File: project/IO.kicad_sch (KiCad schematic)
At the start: 15 parts, among them SW1 CARRIER, SW2 PORT B, SW3 INTERRUPT, X1 PORT B, X2 EXPANSION

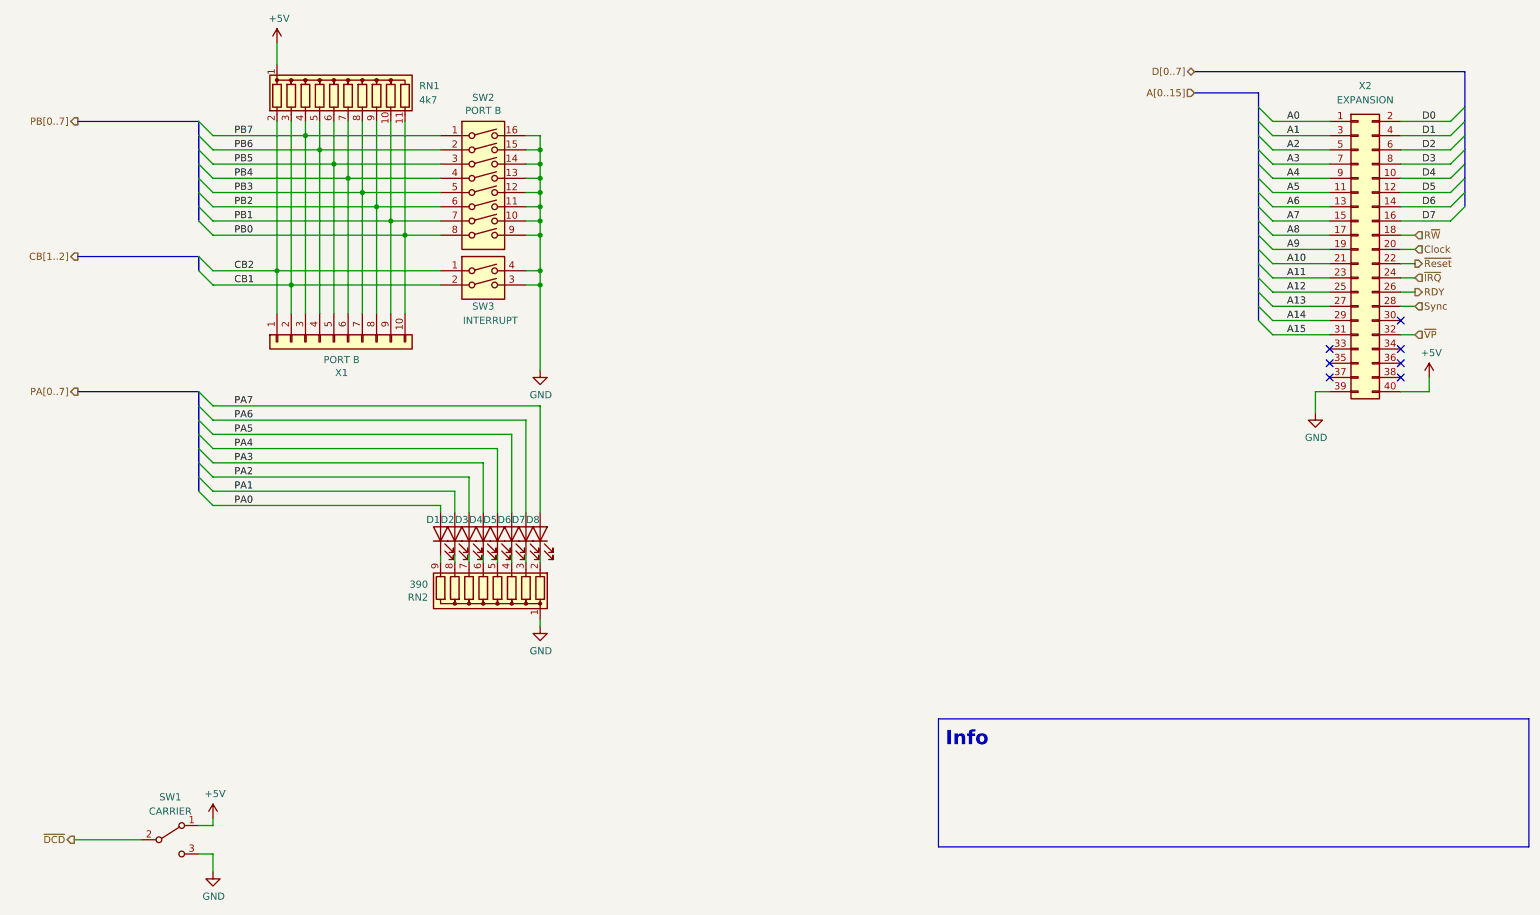
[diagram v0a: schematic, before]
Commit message: Fix grid issues, fix missing libraries, replace FT232 with FT231
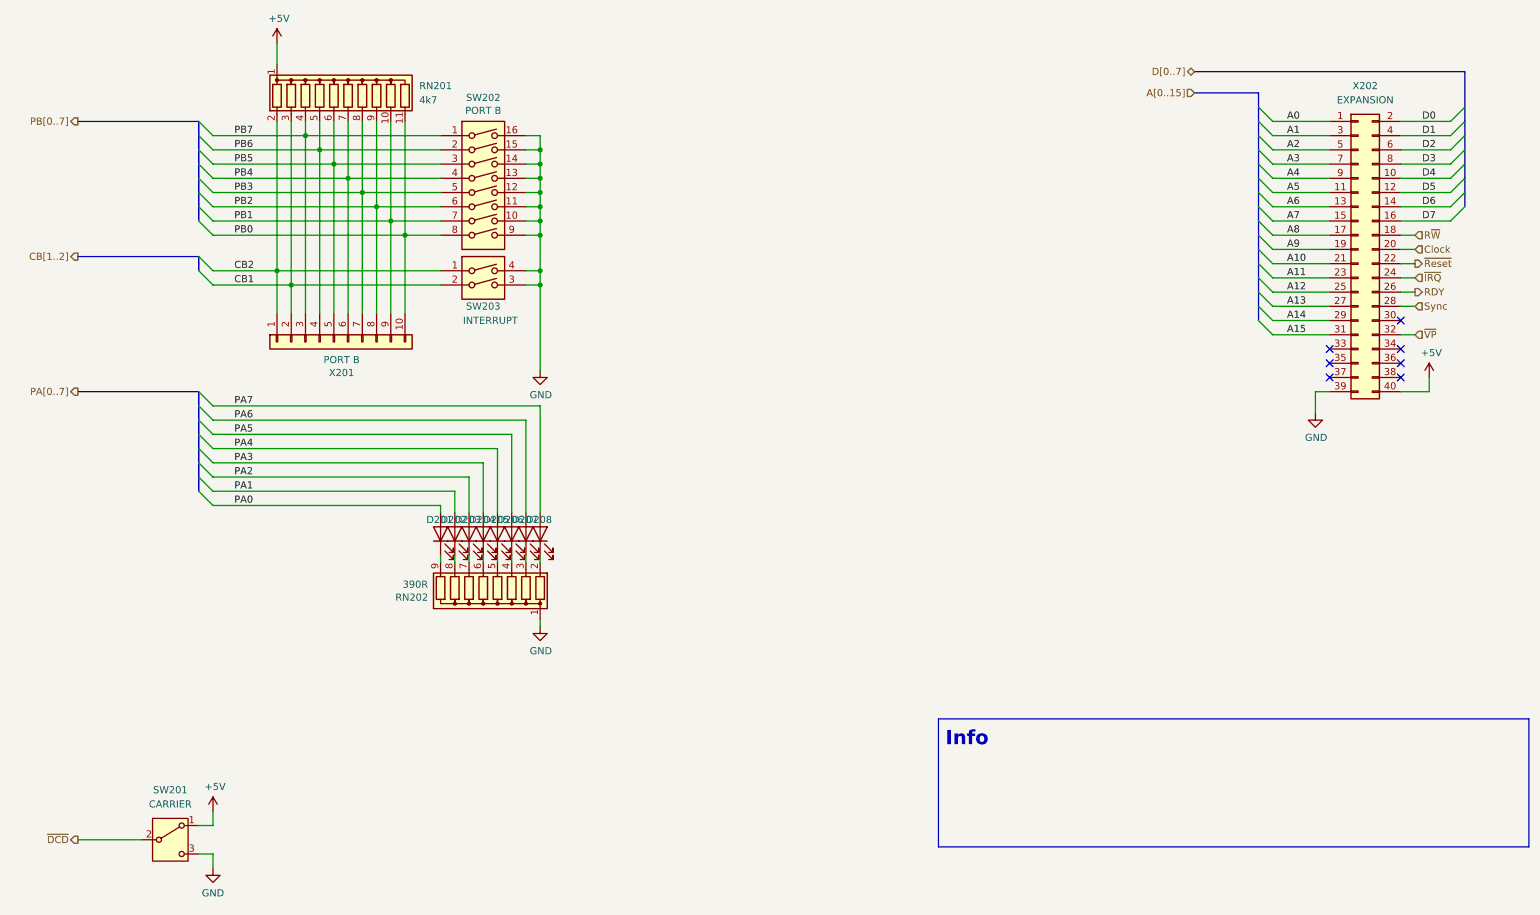
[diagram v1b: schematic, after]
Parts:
- RN202: renamed from RN2; value 390 -> 390R
- renumbered D1 to D201, D2 to D202, D3 to D203, D4 to D204, D5 to D205, D6 to D206, D7 to D207, D8 to D208, RN1 to RN201, SW1 to SW201, SW2 to SW202, SW3 to SW203, X1 to X201, X2 to X202

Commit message: Fix swapped DM and DP, add missing datasheets, remove Mouser property
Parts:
- D201, D202, D203, D204, D205, D206, D207, D208: Mouser 941-C503BRANCZ0C0AA1 -> (none)
- RN201: Mouser 652-4611M-1LF-4.7K -> (none)
- RN202: Mouser 652-4609X-1LF-390 -> (none)
- SW201: Mouser 612-EG1224 -> (none)
- SW202: Mouser 113-NDI08SV -> (none)
- SW203: Mouser 113-NDI02SV -> (none)
- X201: Mouser 571-1-825433-0 -> (none)
- X202: Mfr. No. 4-103328-5 -> 7-146256-0; Mouser 571-4-103328-5 -> (none); Order Number 571-4-103328-5 -> 571-7-146256-0
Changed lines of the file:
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@@
 			)
 		)
-		(property "Datasheet" "~"
+		(property "Datasheet" "https://www.mouser.de/datasheet/2/418/9/ENG_CD_146256_H1-2007701.pdf"
 			(at 252.73 57.15 0)
 			(effects
@@
 			)
 		)
-		(property "Mfr. No." "4-103328-5"
-			(at 252.73 57.15 0)
-			(effects
-				(font
-					(size 1.27 1.27)
-				)
-				(hide yes)
-			)
-		)
-		(property "Mouser" "571-4-103328-5"
+		(property "Mfr. No." "7-146256-0"
 			(at 252.73 57.15 0)
 			(effects
@@
 			)
 		)
-		(property "Order Number" "571-4-103328-5"
+		(property "Order Number" "571-7-146256-0"
+			(at 252.73 57.15 0)
+			(effects
+				(font
+					(size 1.27 1.27)
+				)
+				(hide yes)
+			)
+		)
+		(property "CONFIG" ""
 			(at 252.73 57.15 0)
 			(effects
@@
 			)
 		)
-		(property "Datasheet" "~"
+		(property "Datasheet" "https://www.mouser.de/datasheet/2/140/EG1224-3452627.pdf"
 			(at 40.64 162.56 0)
 			(effects
@@
 		)
 		(property "Mfr. No." "EG1224"
-			(at 40.64 162.56 0)
-			(effects
-				(font
-					(size 1.27 1.27)
-				)
-				(hide yes)
-			)
-		)
-		(property "Mouser" "612-EG1224"
 			(at 40.64 162.56 0)
 			(effects
@@
 			)
 		)
-		(property "Datasheet" "~"
+		(property "Datasheet" "https://www.mouser.de/datasheet/2/418/7/ENG_CD_825433_S_baseFilename-2068609.pdf"
 			(at 69.85 73.66 0)
 			(effects
@@
 		)
 		(property "Mfr. No." "1-825433-0"
-			(at 69.85 73.66 0)
-			(effects
-				(font
-					(size 1.27 1.27)
-				)
-				(hide yes)
-			)
-		)
-		(property "Mouser" "571-1-825433-0"
 			(at 69.85 73.66 0)
 			(effects
@@
 			)
 		)
-		(property "Datasheet" "~"
+		(property "Datasheet" "https://www.mouser.de/datasheet/2/723/HB_C503B_RAS_RAN_AAS_AAN_RBS_RBN_ABS_ABN_RCS_RCN_A-3402026.pdf"
 			(at 106.68 107.95 0)
 			(effects
@@
 		)
 		(property "Mfr. No." "C503B-RAN-CZ0C0AA1"
-			(at 106.68 107.95 0)
-			(effects
-				(font
-					(size 1.27 1.27)
-				)
-				(hide yes)
-			)
-		)
-		(property "Mouser" "941-C503BRANCZ0C0AA1"
 			(at 106.68 107.95 0)
 			(effects
@@
 			)
 		)
-		(property "Datasheet" "~"
+		(property "Datasheet" "https://www.mouser.de/datasheet/2/723/HB_C503B_RAS_RAN_AAS_AAN_RBS_RBN_ABS_ABN_RCS_RCN_A-3402026.pdf"
 			(at 104.14 107.95 0)
 			(effects
@@
 		)
 		(property "Mfr. No." "C503B-RAN-CZ0C0AA1"
-			(at 104.14 107.95 0)
-			(effects
-				(font
-					(size 1.27 1.27)
-				)
-				(hide yes)
-			)
-		)
-		(property "Mouser" "941-C503BRANCZ0C0AA1"
 			(at 104.14 107.95 0)
 			(effects
@@
 			)
 		)
-		(property "Datasheet" "~"
+		(property "Datasheet" "https://www.mouser.de/datasheet/2/723/HB_C503B_RAS_RAN_AAS_AAN_RBS_RBN_ABS_ABN_RCS_RCN_A-3402026.pdf"
 			(at 101.6 107.95 0)
 			(effects
@@
 		)
 		(property "Mfr. No." "C503B-RAN-CZ0C0AA1"
-			(at 101.6 107.95 0)
-			(effects
-				(font
-					(size 1.27 1.27)
-				)
-				(hide yes)
-			)
-		)
-		(property "Mouser" "941-C503BRANCZ0C0AA1"
 			(at 101.6 107.95 0)
 			(effects
@@
 			)
 		)
-		(property "Datasheet" "~"
+		(property "Datasheet" "https://www.mouser.de/datasheet/2/723/HB_C503B_RAS_RAN_AAS_AAN_RBS_RBN_ABS_ABN_RCS_RCN_A-3402026.pdf"
 			(at 99.06 107.95 0)
 			(effects
@@
 		)
 		(property "Mfr. No." "C503B-RAN-CZ0C0AA1"
-			(at 99.06 107.95 0)
-			(effects
-				(font
-					(size 1.27 1.27)
-				)
-				(hide yes)
-			)
-		)
-		(property "Mouser" "941-C503BRANCZ0C0AA1"
 			(at 99.06 107.95 0)
 			(effects
@@
 			)
 		)
-		(property "Datasheet" "~"
+		(property "Datasheet" "https://www.mouser.de/datasheet/2/723/HB_C503B_RAS_RAN_AAS_AAN_RBS_RBN_ABS_ABN_RCS_RCN_A-3402026.pdf"
 			(at 96.52 107.95 0)
 			(effects
@@
 		)
 		(property "Mfr. No." "C503B-RAN-CZ0C0AA1"
-			(at 96.52 107.95 0)
-			(effects
-				(font
-					(size 1.27 1.27)
-				)
-				(hide yes)
-			)
-		)
-		(property "Mouser" "941-C503BRANCZ0C0AA1"
 			(at 96.52 107.95 0)
 			(effects
@@
 			)
 		)
-		(property "Datasheet" "~"
+		(property "Datasheet" "https://www.mouser.de/datasheet/2/723/HB_C503B_RAS_RAN_AAS_AAN_RBS_RBN_ABS_ABN_RCS_RCN_A-3402026.pdf"
 			(at 93.98 107.95 0)
 			(effects
@@
 		)
 		(property "Mfr. No." "C503B-RAN-CZ0C0AA1"
-			(at 93.98 107.95 0)
-			(effects
-				(font
-					(size 1.27 1.27)
-				)
-				(hide yes)
-			)
-		)
-		(property "Mouser" "941-C503BRANCZ0C0AA1"
 			(at 93.98 107.95 0)
 			(effects
@@
 			)
 		)
-		(property "Datasheet" "~"
+		(property "Datasheet" "https://www.mouser.de/datasheet/2/723/HB_C503B_RAS_RAN_AAS_AAN_RBS_RBN_ABS_ABN_RCS_RCN_A-3402026.pdf"
 			(at 91.44 107.95 0)
 			(effects
@@
 		)
 		(property "Mfr. No." "C503B-RAN-CZ0C0AA1"
-			(at 91.44 107.95 0)
-			(effects
-				(font
-					(size 1.27 1.27)
-				)
-				(hide yes)
-			)
-		)
-		(property "Mouser" "941-C503BRANCZ0C0AA1"
 			(at 91.44 107.95 0)
 			(effects
@@
 			)
 		)
-		(property "Datasheet" "~"
+		(property "Datasheet" "https://www.mouser.de/datasheet/2/723/HB_C503B_RAS_RAN_AAS_AAN_RBS_RBN_ABS_ABN_RCS_RCN_A-3402026.pdf"
 			(at 88.9 107.95 0)
 			(effects
@@
 		)
 		(property "Mfr. No." "C503B-RAN-CZ0C0AA1"
-			(at 88.9 107.95 0)
-			(effects
-				(font
-					(size 1.27 1.27)
-				)
-				(hide yes)
-			)
-		)
-		(property "Mouser" "941-C503BRANCZ0C0AA1"
 			(at 88.9 107.95 0)
 			(effects
@@
 			)
 		)
-		(property "Mouser" "652-4609X-1LF-390"
-			(at 96.52 118.11 0)
-			(effects
-				(font
-					(size 1.27 1.27)
-				)
-				(hide yes)
-			)
-		)
 		(property "Distributor" "Mouser"
 			(at 96.52 118.11 0)
@@
 			)
 		)
-		(property "Datasheet" "~"
+		(property "Datasheet" "https://www.mouser.de/datasheet/2/910/DIPT_S_A0003528786_1-2576118.pdf"
 			(at 96.52 46.99 0)
 			(effects
@@
 			)
 		)
-		(property "Mouser" "113-NDI08SV"
-			(at 96.52 46.99 0)
-			(effects
-				(font
-					(size 1.27 1.27)
-				)
-				(hide yes)
-			)
-		)
 		(property "Distributor" "Mouser"
 			(at 96.52 46.99 0)
@@
 		)
 		(property "Order Number" "113-NDI08SV"
+			(at 96.52 46.99 0)
+			(effects
+				(font
+					(size 1.27 1.27)
+				)
+				(hide yes)
+			)
+		)
+		(property "CONFIG" ""
 			(at 96.52 46.99 0)
 			(effects
@@
 			)
 		)
-		(property "Datasheet" "~"
+		(property "Datasheet" "https://www.mouser.de/datasheet/2/910/371_NDI-1571503.pdf"
 			(at 96.52 63.5 0)
 			(effects
@@
 			)
 		)
-		(property "Mouser" "113-NDI02SV"
-			(at 96.52 63.5 0)
-			(effects
-				(font
-					(size 1.27 1.27)
-				)
-				(hide yes)
-			)
-		)
 		(property "Distributor" "Mouser"
 			(at 96.52 63.5 0)
@@
 		)
 		(property "Order Number" "113-NDI02SV"
+			(at 96.52 63.5 0)
+			(effects
+				(font
+					(size 1.27 1.27)
+				)
+				(hide yes)
+			)
+		)
+		(property "CONFIG" ""
 			(at 96.52 63.5 0)
 			(effects
@@
 			(at 72.39 29.21 0)
 			(effects
-				(font
-					(size 1.27 1.27)
-				)
-				(hide yes)
-			)
-		)
-		(property "Mouser" "652-4611M-1LF-4.7K "
-			(at 72.39 29.21 0)
-			(effects
